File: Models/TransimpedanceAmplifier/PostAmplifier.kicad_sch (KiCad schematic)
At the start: 14 parts, among them Q1 Q_PNP, Q2 Q_NPN, U6 OP37GSZ

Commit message: Save progress
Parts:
- removed D4, D5: D, symbol Device:D
- removed R10: 10k, 1%, symbol Device:R_US
- added JP1: Jumper_2_Bridged, symbol Jumper:Jumper_2_Bridged
- added R11: 1k, 1%, symbol Device:R_US
- added R2: 15k, 1%, symbol Device:R_US
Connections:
- net Clamped: now also JP1.2 (B)
- net GND: now also R11.1
- net Output: now also R2.2
- net at U6.2 (-IN): now also JP1.1 (A), R11.2, R2.1
- net Input: now reaches U6.3 (+IN)
- no-connect marks 1 -> 3
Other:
- note added: "Alternative to the 15k feedback resistor at high voltage"
- note added: "Cannot "suppress the influence of transistor leakage currents or parasitic capacitances on the input of OP2" b/c the connection point is a nonzero voltage instead of GND with this design. The approach used in the original paper would make the diodes conduct from the voltage differential between the connection point and (10k) * (±25 nA) ≈ (±0.25 mV). Instead, provide a reversible (THT) jumper to d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"
- moved on the sheet: D2, D3, D6, D7, Q1, Q2, R6, R7, R8, R9, U6

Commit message: Got the purchase links for the remaining discrete devices in this task
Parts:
- D2, D3: Purchase Link (none) -> https://www.digikey.com/en/products/detail/texas-instrument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
- D6, D7: Purchase Link (none) -> https://www.digikey.com/en/products/detail/vishay-general-s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
- Q1: Purchase Link (none) -> https://www.digikey.com/en/products/detail/onsemi/MMBT2907A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
- Q2: Purchase Link (none) -> https://www.digikey.com/en/products/detail/onsemi/MMBT2222A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
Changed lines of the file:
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@@
+			)
+		)
+		(property "Purchase Link" "https://www.digikey.com/en/products/detail/onsemi/MMBT2907ALT1G/919599"
+			(at 236.22 76.2 0)
+			(effects
+				(font
+					(size 1.27 1.27)
+				)
+				(hide yes)
 			)
 		)
@@
 			)
 		)
+		(property "Purchase Link" "https://www.digikey.com/en/products/detail/onsemi/MMBT2222ALT1G/919593"
+			(at 236.22 119.38 0)
+			(effects
+				(font
+					(size 1.27 1.27)
+				)
+				(hide yes)
+			)
+		)
 		(pin "C"
 		)
@@
 			)
 		)
+		(property "Purchase Link" "https://www.digikey.com/en/products/detail/vishay-general-semiconductor-diodes-division/1N4448W-E3-08/4829905"
+			(at 224.79 66.04 0)
+			(effects
+				(font
+					(size 1.27 1.27)
+				)
+				(hide yes)
+			)
+		)
 		(pin "1"
 		)
@@
 			)
 		)
+		(property "Purchase Link" "https://www.digikey.com/en/products/detail/texas-instruments/LM4040D10IDBZR/1216503"
+			(at 241.3 82.55 90)
+			(effects
+				(font
+					(size 1.27 1.27)
+				)
+				(hide yes)
+			)
+		)
 		(pin "1"
 		)
@@
 			)
 		)
+		(property "Purchase Link" "https://www.digikey.com/en/products/detail/vishay-general-semiconductor-diodes-division/1N4448W-E3-08/4829905"
+			(at 224.79 129.54 0)
+			(effects
+				(font
+					(size 1.27 1.27)
+				)
+				(hide yes)
+			)
+		)
 		(pin "1"
 		)
@@
 			(effects
 				(font
+					(size 1.27 1.27)
+				)
+				(hide yes)
+			)
+		)
+		(property "Purchase Link" "https://www.digikey.com/en/products/detail/texas-instruments/LM4040D10IDBZR/1216503"
+			(at 241.3 110.49 90)
+			(effects
+				(font

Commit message: All suppliers are out of stock of LM7915L in the simple TO-92-3 package. Resolve this by first tabulating the maximum possible current on each regulator.
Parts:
- U6: Purchase Link (none) -> https://www.mouser.com/ProductDetail/Analog-Devices/OP37GSZ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
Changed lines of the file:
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@@
+			)
+		)
+		(property "Purchase Link" "https://www.mouser.com/ProductDetail/Analog-Devices/OP37GSZ?qs=WIvQP4zGangnlHcCmYh5ww%3D%3D"
+			(at 71.12 73.66 0)
+			(effects
+				(font
+					(size 1.27 1.27)
+				)
+				(hide yes)
 			)
 		)

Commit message: Refactoring in progress
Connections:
- net Feedback_Terminal: now reaches JP1.1 (A), R11.2, R2.1, U6.2 (-IN)
- net Clamped renamed Clamped_Output
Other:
- moved on the sheet: JP1, R11, R2, U6

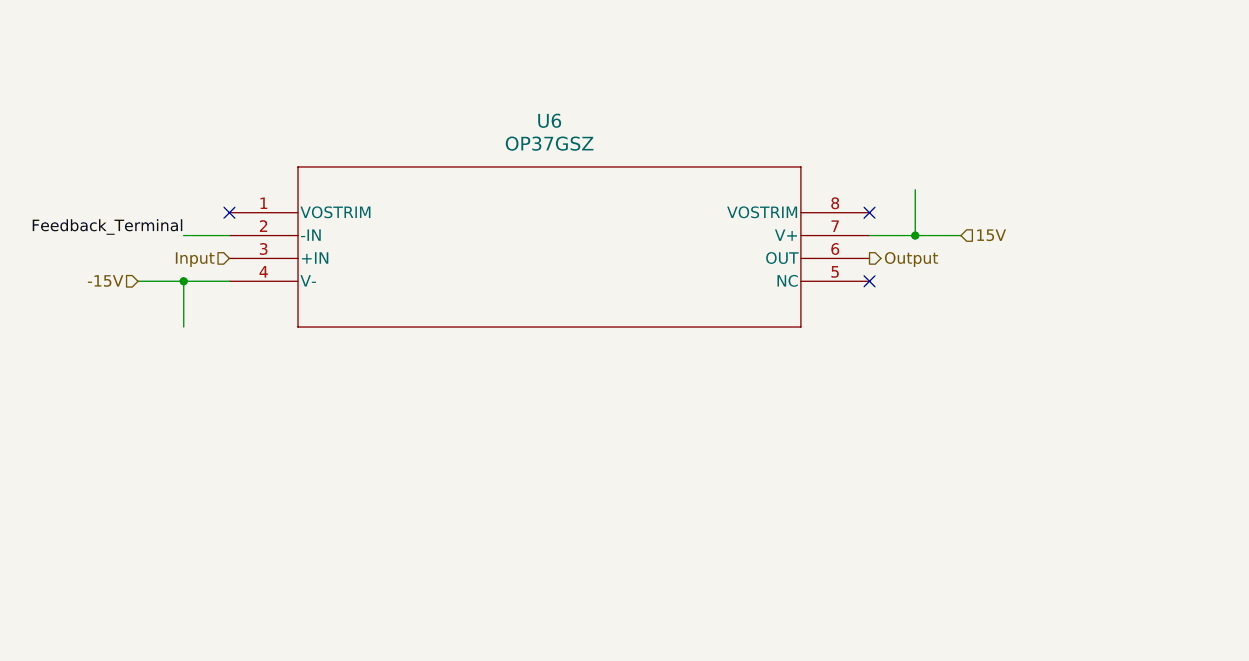
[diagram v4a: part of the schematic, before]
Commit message: Finished the decoupling networks for the power subsystem
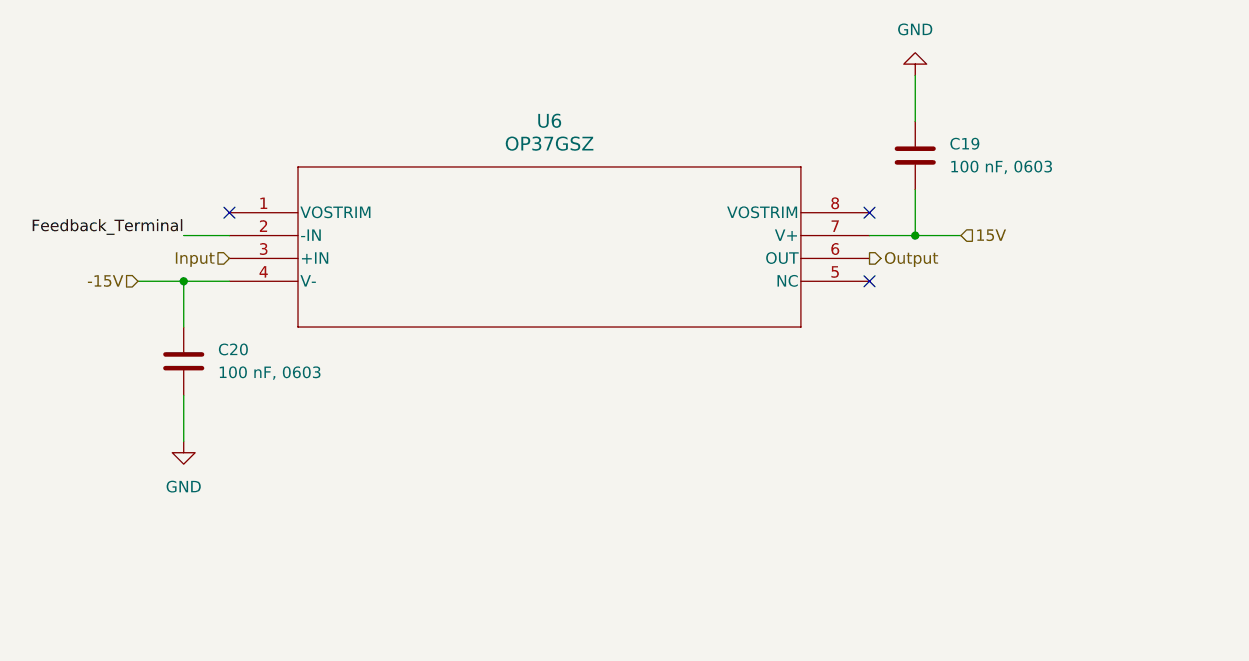
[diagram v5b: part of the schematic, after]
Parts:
- added C19, C20: 100 nF, 0603, symbol Device:C
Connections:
- net -15V: now also C20.1
- net 15V: now also C19.2
- net GND: now also C19.1, C20.2

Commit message: Finished for today
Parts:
- C19, C20: Purchase Link (none) -> https://www.digikey.com/en/products/detail/murata-electroni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
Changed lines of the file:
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@@
 			)
 		)
-		(property "Purchase Link" ""
+		(property "Purchase Link" "https://www.digikey.com/en/products/detail/murata-electronics/GRM188R72A104KA35D/702549"
 			(at 137.16 54.61 0)
 			(effects
@@
 			)
 		)
-		(property "Purchase Link" ""
+		(property "Purchase Link" "https://www.digikey.com/en/products/detail/murata-electronics/GRM188R72A104KA35D/702549"
 			(at 55.88 77.47 0)
 			(effects

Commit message: Save progress
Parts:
- removed Q1: Q_PNP, symbol Device:Q_PNP
- removed Q2: Q_NPN, symbol Device:Q_NPN
- added Q3: Q_PNP, symbol Custom:Q_PNP
- added Q4: Q_NPN, symbol Custom:Q_NPN
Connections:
- net Clamped_Output: now also Q3.3 (C), Q4.3 (C)
- net at D6.1 (K): now also Q3.2 (E)
- net at D7.2 (A): now also Q4.2 (E)
- net -10V: no longer names the net of D3.2 (A), R9.1
- net -10V: now also Q4.1 (B)
- net 10V: no longer names the net of D2.1 (K), R7.2
- net 10V: now also Q3.1 (B)
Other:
- moved on the sheet: D2, D3, R6, R7, R8, R9

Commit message: Save progress
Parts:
- removed D2, D3: 10V, 1%, symbol Device:D_Zener
- added D2, D3: 10V, 1%, symbol Custom:D_Zener
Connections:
- net GND: now also D2.2 (A), D2.3 (*), D3.1 (K)
- net at Q3.1 (B), R7.2: now also D2.1 (K)
- net at Q4.1 (B), R9.1: now also D3.2 (A), D3.3 (*)
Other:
- moved on the sheet: D6, D7, Q3, Q4, R6, R8
